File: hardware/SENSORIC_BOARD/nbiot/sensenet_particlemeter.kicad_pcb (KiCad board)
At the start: 2 copper layers, 63.6 x 72.4 mm, 102 parts, among them J1 CONN_01X01, J11 CONN_01X01, J13 BARREL_JACK, J18 CONN_01X01, J19 CONN_01X01, J2 CONN_01X01, J21 CONN_01X01, J3 CONN_01X01, J4 CONN_01X01, J5 CONN_01X01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

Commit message: snazim se rozchodit novou serii, jebne me z toho z chvili
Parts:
- added C24: 2.2u, SNPM:SMD_0805, F.Cu at (182.6, 105.9)
- added J10: CONN_01X01, SNPM:smd_point_bottom, F.Cu at (177.2, 86.4)
- added J12: CONN_01X01, SNPM:smd_point_bottom, F.Cu at (179.8, 86.4)
- added J14: CONN_01X01, SNPM:smd_point_bottom, F.Cu at (182.3, 86.4)
- added J15: CONN_01X01, SNPM:smd_point_bottom, F.Cu at (184.8, 86.4)
- added J7: CONN_01X01, SNPM:smd_point_bottom, F.Cu at (169.6, 86.4)
- added J8: CONN_01X01, SNPM:smd_point_bottom, F.Cu at (172.1, 86.4)
- added J9: CONN_01X01, SNPM:smd_point_bottom, F.Cu at (174.7, 86.4)
- moved J6 1.64 mm to (171.6, 59.5)
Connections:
- U9 pad 28: (no net) -> Net-(C24-Pad1)
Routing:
- net OLED_RESET: track 11.1 -> 58.9 mm, vias 1 -> 3
- net OLED_D/C: track 8.82 -> 53.1 mm, vias 1 -> 5
- net OLED_CS: track 13.1 -> 51.2 mm, vias 1 -> 3
- net +5V: track 92.3 -> 111.7 mm, vias 2 -> 4
- net PM_SCK: track 29.2 -> 39.9 mm, vias 1 -> 2
- net PM_SDO: track 35.7 -> 45.1 mm, vias 1 -> 2
- net Net-(C24-Pad1): track 0.00 -> 6.49 mm, vias 0 -> 1
- net Net-(D8-Pad2): track 19.5 -> 23.8 mm
- net GND: track 156.7 -> 160.8 mm, vias 47 -> 49
- net Net-(D9-Pad2): track 19.4 -> 22.6 mm
- net Net-(D10-Pad2): track 18.0 -> 21.1 mm
- net (no net): track 0.00 -> 2.71 mm, vias 0 -> 3
- net +3V3: track 287.1 -> 289.4 mm
- net i2c_sda: track 75.7 -> 77.8 mm
- net i2c_scl: track 69.7 -> 71.8 mm
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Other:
- rule via_min_drill: 0.3 -> 0.4
- rule via_min_size: 0.4 -> 0.6

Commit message: rozdelane upravicky
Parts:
- added C26: 1n, Capacitor_SMD:C_0805_2012Metric, F.Cu at (159.7, 122.7)
- added C27: 1n, Capacitor_SMD:C_0805_2012Metric, F.Cu at (159.7, 124.7)
- added C28: 22p, Capacitor_SMD:C_0805_2012Metric, F.Cu at (150.8, 118.9)
- added L9: 39uH, Inductor_SMD:L_Taiyo-Yuden_NR-50xx, F.Cu at (190.9, 132.6)
- added R30: 0R, Resistor_SMD:R_0805_2012Metric, F.Cu at (164.0, 60.7)
- C12: value 510pF -> 330pF
- C13: value C -> 100n
- C15: value 1000u -> 470u; footprint SNPM:C_Radial_D10_L16_P5_bottom -> Capacitor_SMD:C_0805_2012Metric
- C17: value 1000u -> 100n; footprint SNPM:C_Radial_D10_L16_P5_bottom -> Capacitor_SMD:C_0805_2012Metric
- C18: footprint SNPM:C_Radial_D6.3_L11.2_P2.5_bottom -> Capacitor_THT:CP_Radial_D10.0mm_P5.00mm
- C19: footprint SNPM:C_Radial_D10_L16_P5_bottom -> Capacitor_THT:CP_Radial_D10.0mm_P5.00mm
- J13: value BARREL_JACK -> Conn_01x02_Female; footprint SNPM:BARREL_JACK -> Connector_Wire:SolderWirePad_1x02_P3.81mm_Drill1.2mm
- L1, L2: value L -> DNP
- R15: value 27k -> 2k7
- R16: value 10k -> 820R
- R21: value tbd -> 100R
- moved C13 52.3 mm to (156.9, 112.5), turned to 90 degrees
- moved C19 20.0 mm to (157.4, 134.1)
- moved D3 13.0 mm to (189.9, 124.5)
- moved J13 9.50 mm to (193.7, 116.9), turned to 270 degrees
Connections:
- C13 pad 1: Net-(C13-Pad1) -> +9V
- C13 pad 2: Net-(C13-Pad2) -> GND
- C7 pad 1: +3V3 -> GND
- C7 pad 2: GND -> +3V3
- D3 pad 1: +9V -> Net-(D3-Pad1)
- J13 pad 1: Net-(D3-Pad2) -> GND
- J13 pad 2: GND -> Net-(D3-Pad2)
- L1 pad 1: Net-(C13-Pad2) -> Net-(L1-Pad1)
- L2 pad 1: Net-(C13-Pad1) -> Net-(L2-Pad1)
- P2 pad 2: Net-(C13-Pad1) -> Net-(L2-Pad1)
- U3 pad 26: +3V3 -> (no net)
- U3 pad 45: batt -> +3V3
- U3 pad 46: batt -> +3V3
- U7 pad 14: (no net) -> +3V3
- U7 pad 3: Net-(C13-Pad2) -> Net-(L1-Pad1)
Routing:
- net Net-(SW3-Pad1): track 25.5 -> 0.00 mm, vias 2 -> 0
- net +9V: track 71.5 -> 47.2 mm
- net +3V3: track 289.4 -> 278.0 mm
- net Net-(D3-Pad2): track 7.59 -> 0.00 mm
- net Net-(C13-Pad1): track 4.94 -> 0.00 mm
- net Net-(C13-Pad2): track 4.74 -> 0.00 mm
- net Net-(C18-Pad1): track 11.2 -> 7.11 mm
- net Net-(D6-Pad1): track 13.2 -> 9.40 mm
- net batt: track 1.10 -> 0.00 mm

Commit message: V5
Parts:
- removed D4: red LED, SNPM:SMD_0805_bottom
- removed D5: 1N5819, SNPM:D_SOD-123
- removed D7: green LED, SNPM:SMD_0805_bottom
- removed L9: 39uH, Inductor_SMD:L_Taiyo-Yuden_NR-50xx
- removed R15: 2k7, SNPM:SMD_0805
- removed R24: tbd, SNPM:SMD_0805
- removed R26: 1k, SNPM:SMD_0805
- removed R3: 8k2, SNPM:SMD_0805
- added C29: 1n, Capacitor_SMD:C_0805_2012Metric, F.Cu at (162.5, 118.6)
- added C30: 47u, Capacitor_SMD:C_0805_2012Metric, F.Cu at (176.8, 119.2)
- C12: value 330pF -> 100n
- C13: value 100n -> 1u
- C15: footprint Capacitor_SMD:C_0805_2012Metric -> Capacitor_THT:CP_Radial_D10.0mm_P5.00mm
- C19: value 1000u -> 470u
- C25: footprint SNPM:SMD_0805 -> Capacitor_SMD:C_0805_2012Metric
- D1: footprint SNPM:SMD_0805 -> Diode_SMD:D_SOD-123
- R12: value 0R33 -> 100k
- R13: value tbd -> 100k
- U1: value MC33063 -> NCP59152; footprint SNPM:SOIC-8_3.9x4.9mm_Pitch1.27mm -> Package_DFN_QFN:DFN-8-1EP_4x4mm_P0.8mm_EP2.39x2.21mm
- moved C28 51.5 mm to (183.5, 79.1), turned to 270 degrees
- moved C27 50.5 mm to (181.4, 79.1), turned to 270 degrees
- moved D1 43.5 mm to (188.1, 79.6), turned to 270 degrees
- moved C25 39.3 mm to (185.6, 79.1), turned to 270 degrees
- moved C7 30.7 mm to (148.6, 60.2), turned to 270 degrees
- moved D6 27.3 mm to (138.9, 95.8), turned to 0 degrees
- moved L7 25.7 mm to (187.0, 119.5)
- moved C26 25.2 mm to (184.6, 119.2), turned to 90 degrees
- moved L5 24.7 mm to (139.0, 100.4), turned to 0 degrees
- moved C16 20.6 mm to (134.5, 107.9), turned to 270 degrees
- moved C17 20.1 mm to (182.0, 119.2), turned to 90 degrees
- moved C12 18.2 mm to (160.4, 118.6), turned to 270 degrees
- moved R19 16.2 mm to (146.6, 108.6), turned to 0 degrees
- moved C19 16.0 mm to (158.0, 118.1), turned to 270 degrees
- moved D11 16.0 mm to (147.9, 123.1), turned to 270 degrees
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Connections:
- C12 pad 1: Net-(C12-Pad1) -> +9V
- L3 pad 1: Net-(D5-Pad1) -> Net-(D3-Pad1)
- L3 pad 2: Net-(L3-Pad2) -> +9V
- L4 pad 2: Net-(L3-Pad2) -> Net-(C30-Pad1)
- R12 pad 1: Net-(R12-Pad1) -> Net-(C30-Pad1)
- R12 pad 2: +9V -> Net-(R12-Pad2)
- R13 pad 1: Net-(R12-Pad1) -> 5V_enable
- R13 pad 2: +9V -> GND
- R16 pad 1: Net-(R15-Pad2) -> Net-(C30-Pad1)
- R23 pad 2: Net-(R23-Pad2) -> GND
- U1 pad 1: Net-(R12-Pad1) -> GND
- U1 pad 2: Net-(D5-Pad1) -> 5V_enable
- U1 pad 3: Net-(C12-Pad1) -> +9V
- U1 pad 4: GND -> (no net)
- U1 pad 5: Net-(R15-Pad2) -> (no net)
- U1 pad 6: +9V -> Net-(C30-Pad1)
- U1 pad 7: Net-(R12-Pad1) -> Net-(R16-Pad2)
- U1 pad 8: Net-(R12-Pad1) -> Net-(R12-Pad2)
- U2 pad 26: (no net) -> 5V_enable
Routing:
- net Net-(SW3-Pad1): track 0.00 -> 23.5 mm, vias 0 -> 2
- net Net-(D7-Pad2): track 21.4 -> 0.00 mm, vias 1 -> 0
- net 5V_enable: track 0.00 -> 18.5 mm
- net Net-(D3-Pad1): track 0.00 -> 18.1 mm
- net Net-(R12-Pad1): track 17.5 -> 0.00 mm, vias 2 -> 0
- net Net-(D4-Pad2): track 16.1 -> 0.00 mm, vias 1 -> 0
- net Net-(D5-Pad1): track 12.9 -> 0.00 mm
- net Net-(C30-Pad1): track 0.00 -> 10.1 mm
- net Net-(R15-Pad2): track 9.53 -> 0.00 mm
- net +5V: track 111.7 -> 119.7 mm, vias 4 -> 3
- net Net-(L5-Pad2): track 7.67 -> 15.3 mm
- net Net-(R16-Pad2): track 1.97 -> 8.88 mm
- net +3V3: track 278.0 -> 271.1 mm
- net Net-(L3-Pad2): track 6.74 -> 0.00 mm
- net Net-(C18-Pad1): track 7.11 -> 13.1 mm
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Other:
- outline, holes or cut-outs redrawn
- net class Default: trace_width 0.15 -> 0.3

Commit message: dalsi updaty
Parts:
- removed C20, C22, C3: C, SNPM:SMD_0805
- removed C24: 2.2u, SNPM:SMD_0805
- removed R25: R, SNPM:SMD_0805
- removed U9: OLED_128x64, SNPM:OLED_display128x64_bottom
- C1: value 2.2u -> 100n; footprint SNPM:SMD_0805 -> Capacitor_SMD:C_0805_2012Metric
- C10, C11, C12, C13, C14, C16, C4, C5, C6, C7, C8, C9: footprint SNPM:SMD_0805 -> Capacitor_SMD:C_0805_2012Metric
- C2: value C -> 22p; footprint SNPM:SMD_0805 -> Capacitor_SMD:C_0805_2012Metric
- C23: value 10u -> 2.2u
- R16: value 820R -> 3k3
- R21: value 100R -> 1k1
- moved C1 38.5 mm to (151.0, 123.6)
- moved C2 22.0 mm to (153.5, 123.6)
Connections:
- C1 pad 1: Net-(C1-Pad1) -> +3V3
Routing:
- net Net-(C20-Pad1): track 10.4 -> 0.00 mm, vias 1 -> 0
- net Net-(C20-Pad2): track 9.15 -> 0.00 mm, vias 1 -> 0
- net Net-(C1-Pad1): track 8.44 -> 0.06 mm, vias 1 -> 0
- net Net-(C22-Pad1): track 7.39 -> 0.00 mm, vias 1 -> 0
- net PM_SDO: track 45.1 -> 38.4 mm
- net Net-(C24-Pad1): track 6.49 -> 0.00 mm, vias 1 -> 0
- net Net-(C22-Pad2): track 5.85 -> 0.00 mm, vias 1 -> 0
- net PM_SCK: track 39.9 -> 35.3 mm
- net Net-(R25-Pad1): track 3.91 -> 0.00 mm, vias 1 -> 0
- net +3V3: track 271.1 -> 273.1 mm
- net GND: track 162.9 -> 161.7 mm, vias 50 -> 49

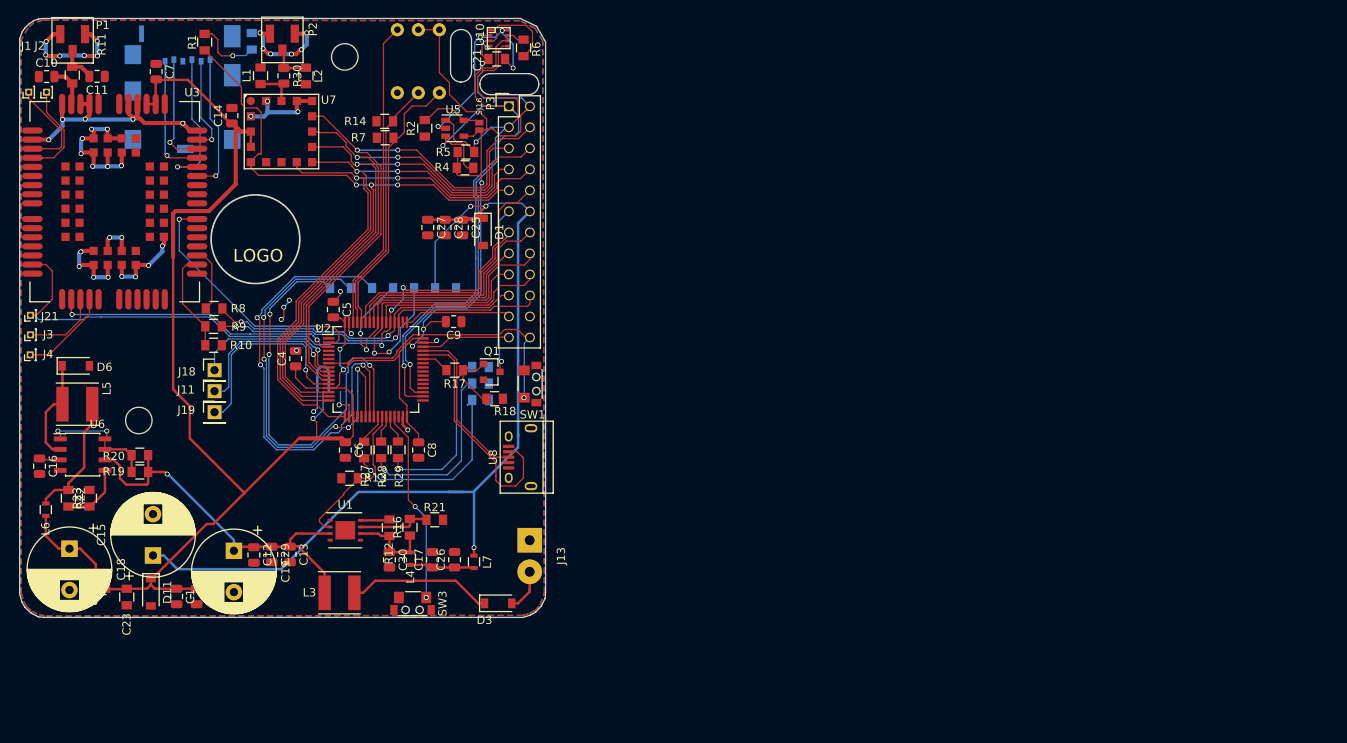
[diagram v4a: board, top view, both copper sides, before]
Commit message: Daily update, rework zdroju - oba dva LDO s adjustem, 5Venable, pico clasp connector, priprava na lorawan shield
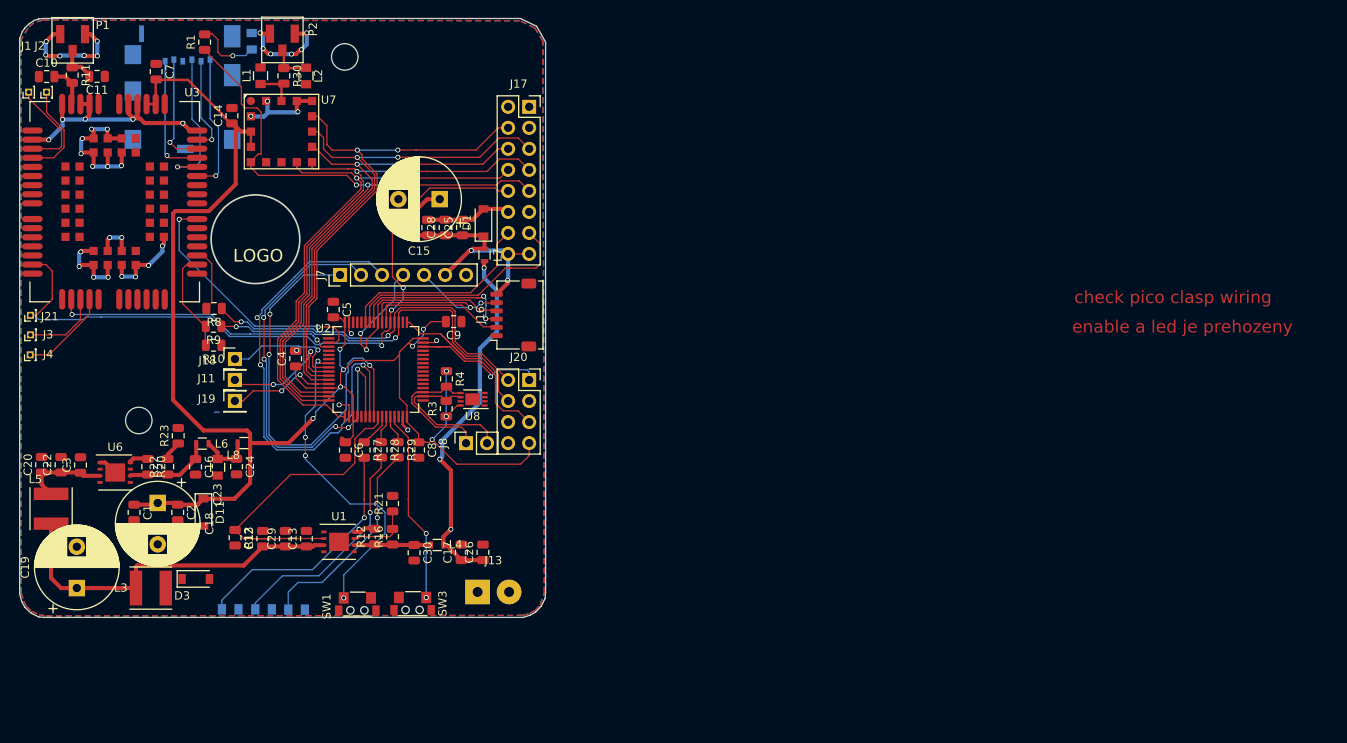
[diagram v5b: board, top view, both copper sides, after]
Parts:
- removed C21: 100n, SNPM:SMD_0805
- removed D6: 1N5819, SNPM:D_SOD-123
- removed J10, J12, J14, J15, J9: CONN_01X01, SNPM:smd_point_bottom
- removed P3: CONN_02X12, SNPM:Pin_Header_Straight_2x12
- removed Q1: Q_NMOS_GSD, SNPM:SOT-23
- removed R14, R7: 10k, SNPM:SMD_0805
- removed R17, R18: R, SNPM:SMD_0805
- removed R19: 0R33, SNPM:SMD_0805
- removed R2, R5: 4.7k, SNPM:SMD_0805
- removed R6: 22k, SNPM:SMD_0805
- removed SJ16: solder_jumper, SNPM:solder_jumper
- removed SW2: SW_DIP_x03, SNPM:DIP-6_W7.62mm_bot
- removed U10: bme280_barebone, SNPM:BME280
- removed U5: CAT24C02, TO_SOT_Packages_SMD:SOT-23-5
- added C20: 100n, Capacitor_SMD:C_0805_2012Metric, F.Cu at (134.7, 107.7)
- added C22: 1n, Capacitor_SMD:C_0805_2012Metric, F.Cu at (137.1, 107.7)
- added C24: 1n, Capacitor_SMD:C_0805_2012Metric, F.Cu at (158.3, 107.9)
- added C3: 22u, Capacitor_SMD:C_0805_2012Metric, F.Cu at (139.4, 107.8)
- added J16: Conn_01x06_Female, molexpico:pico_clasp_6_horizontal, F.Cu at (191.7, 89.6)
- added J17: Conn_02x08_Odd_Even, Connector_PinSocket_2.54mm:PinSocket_2x08_P2.54mm_Vertical, F.Cu at (193.7, 64.5)
- added J20: Conn_02x04_Odd_Even, Connector_PinSocket_2.54mm:PinSocket_2x04_P2.54mm_Vertical, F.Cu at (193.7, 97.5)
- added R3: 4k7, Resistor_SMD:R_0805_2012Metric, F.Cu at (183.6, 101.0)
- C13: value 1u -> 22u
- C16: value 352pF -> 47u
- C23: value 2.2u -> 100n
- J7: value CONN_01X01 -> Conn_01x07_Female; footprint SNPM:smd_point_bottom -> Connector_PinHeader_2.54mm:PinHeader_1x07_P2.54mm_Vertical
- J8: value CONN_01X01 -> Conn_01x02_Female; footprint SNPM:smd_point_bottom -> Connector_PinSocket_2.54mm:PinSocket_1x02_P2.54mm_Vertical
- R1, R10, R11, R12, R13, R16, R21, R22, R23, R27, R28, R29, R8, R9: footprint SNPM:SMD_0805 -> Resistor_SMD:R_0805_2012Metric
- R20: value tbd -> 100k; footprint SNPM:SMD_0805 -> Resistor_SMD:R_0805_2012Metric
- R4: value 4.7k -> 4k7; footprint SNPM:SMD_0805 -> Resistor_SMD:R_0805_2012Metric
- U6: value MC33063 -> NCP59152; footprint Housings_SOIC:SOIC-8_3.9x4.9mm_Pitch1.27mm -> Package_DFN_QFN:DFN-8-1EP_4x4mm_P0.8mm_EP2.39x2.21mm
- U8: value usb_femalee -> ATECC508A; footprint Connectors:USB_Micro-B -> Package_DFN_QFN:DFN-8-1EP_3x2mm_P0.5mm_EP1.75x1.45mm
- moved C15 55.3 mm to (182.8, 75.6), turned to 180 degrees
- moved D8 39.4 mm to (157.5, 125.2)
- moved D9 37.8 mm to (161.6, 125.2)
- moved L7 37.1 mm to (188.3, 82.4)
- moved D10 36.8 mm to (165.5, 125.2)
- moved D3 36.7 mm to (153.4, 121.5)
- moved SW1 33.5 mm to (172.8, 124.3), turned to 180 degrees
- moved R4 25.6 mm to (183.7, 97.3), turned to 270 degrees
- moved L8 24.6 mm to (159.2, 105.1)
- moved J8 23.3 mm to (186.0, 105.1), turned to 90 degrees
- moved L3 22.8 mm to (147.9, 122.6)
- moved L6 20.5 mm to (154.2, 105.2), turned to 180 degrees
- moved C19 19.5 mm to (139.0, 122.6), turned to 90 degrees
- moved C23 19.1 mm to (156.0, 108.0)
- moved C16 18.9 mm to (153.3, 108.0)
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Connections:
- C12 pad 1: +9V -> +6V
- C13 pad 1: +9V -> +6V
- C18 pad 1: Net-(C18-Pad1) -> +3V3
- C19 pad 1: +9V -> +6V
- C23 pad 1: +3V3 -> Net-(C23-Pad1)
- C29 pad 1: +9V -> +6V
- J8 pad 1: OLED_D/C -> i2c_sda
- L3 pad 2: +9V -> +6V
- L5 pad 1: Net-(D6-Pad1) -> +6V
- L5 pad 2: Net-(L5-Pad2) -> Net-(C20-Pad1)
- L6 pad 1: Net-(C18-Pad1) -> Net-(C23-Pad1)
- L6 pad 2: Net-(L5-Pad2) -> Net-(C16-Pad1)
- L8 pad 2: Net-(C18-Pad1) -> Net-(C23-Pad1)
- R20 pad 1: Net-(R19-Pad1) -> Net-(R20-Pad1)
- R20 pad 2: +9V -> Net-(C16-Pad1)
- R22 pad 1: Net-(L5-Pad2) -> Net-(C16-Pad1)
- R4 pad 1: i2c_sda -> +3V3
- R4 pad 2: +3V3 -> i2c_sda
- U1 pad 3: +9V -> +6V
- U2 pad 25: Net-(R27-Pad1) -> 5V_enable
- U2 pad 26: 5V_enable -> Net-(R27-Pad1)
- U2 pad 43: PM_meter_switch -> (no net)
- U2 pad 44: PA11-USB-DM -> (no net)
- U2 pad 45: PA12-USB-DP -> (no net)
- U2 pad 60: BOOT_0 -> (no net)
- U2 pad 61: BOOT_signal -> (no net)
- U2 pad 62: debug_on_off -> (no net)
- U6 pad 1: Net-(R19-Pad1) -> GND
- U6 pad 2: Net-(D6-Pad1) -> (no net)
- U6 pad 3: Net-(C16-Pad1) -> Net-(C20-Pad1)
- U6 pad 4: GND -> (no net)
- U6 pad 5: Net-(R22-Pad2) -> (no net)
- U6 pad 6: +9V -> Net-(C16-Pad1)
- U6 pad 7: Net-(R19-Pad1) -> (no net)
- U6 pad 8: Net-(R19-Pad1) -> Net-(R20-Pad1)
- U8 pad 1: GND -> (no net)
- U8 pad 3: PA12-USB-DP -> (no net)
- U8 pad 4: PA11-USB-DM -> GND
- U8 pad 5: (no net) -> i2c_sda
- U8 pad 6: GND -> i2c_scl
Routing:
- net +5V: track 119.7 -> 37.2 mm, vias 3 -> 2
- net +3V3: track 273.1 -> 193.8 mm, vias 7 -> 9
- net i2c_sda: track 77.8 -> 16.9 mm, vias 2 -> 0
- net i2c_scl: track 71.8 -> 19.2 mm, vias 2 -> 0
- net +9V: track 46.7 -> 0.00 mm, vias 1 -> 0
- net +6V: track 0.00 -> 43.7 mm
- net debug_on_off: track 37.6 -> 0.00 mm
- net Net-(C17-Pad1): track 7.90 -> 44.3 mm, vias 0 -> 3
- net BOOT_0: track 33.3 -> 0.00 mm
- net BOOT_signal: track 31.0 -> 0.00 mm
- net PA11-USB-DM: track 29.3 -> 0.00 mm
- net GND: track 161.7 -> 135.2 mm, vias 49 -> 42
- net NMOS: track 20.1 -> 0.00 mm, vias 1 -> 0
- net PA12-USB-DP: track 19.9 -> 0.00 mm
- net 5V_enable: track 18.5 -> 37.8 mm
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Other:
- outline, holes or cut-outs redrawn
- net class Default: trace_width 0.3 -> 0.15
- board text added: "check pico clasp wiring"
- board text added: "enable a led je prehozeny"

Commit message: daily, jeste musim prehodit gps doprava
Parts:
- moved J13 4.45 mm to (191.9, 122.9), turned to 180 degrees
- moved R10 2.51 mm to (157.2, 91.5)
- moved R9 2.31 mm to (157.2, 89.4)
- moved C6 2.29 mm to (169.4, 104.9)
- moved R8 2.21 mm to (157.2, 87.3)
- moved C4 0.21 mm to (165.2, 94.9)
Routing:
- net Net-(D3-Pad2): track 0.00 -> 33.6 mm
- net GND: track 135.2 -> 166.5 mm, vias 42 -> 58
- net OLED_CS: track 52.5 -> 39.9 mm
- net OLED_D/C: track 55.1 -> 44.3 mm, vias 5 -> 3
- net OLED_RESET: track 60.8 -> 50.2 mm
- net +3V3: track 193.8 -> 188.4 mm, vias 9 -> 7
- net PM_SDO: track 32.6 -> 28.1 mm, vias 2 -> 1
- net Net-(J11-Pad1): track 15.9 -> 12.9 mm, vias 2 -> 1
- net Net-(D8-Pad2): track 29.8 -> 32.7 mm
- net 5V_enable: track 37.8 -> 40.3 mm
- net Net-(D3-Pad1): track 0.00 -> 2.43 mm
- net Net-(R10-Pad2): track 12.4 -> 10.3 mm
- net Net-(R8-Pad2): track 7.91 -> 6.51 mm
- net Net-(J18-Pad1): track 15.1 -> 13.7 mm
- net Net-(D10-Pad2): track 25.6 -> 26.7 mm
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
